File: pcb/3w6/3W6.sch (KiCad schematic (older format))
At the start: 115 parts, among them J1 USB_C Main, J2 USB_C I2C_L, J3 USB_C I2C_R, SW1 SW_Push, SW10 SW_Push, SW11 SW_Push, SW12 SW_Push, SW13 SW_Push, SW14 SW_Push, SW15 SW_Push, SW16 SW_Push, SW17 SW_Push, SW18 SW_Push, SW19 SW_Push, SW2 SW_Push, SW20 SW_Push, SW21 SW_Push, SW22 SW_Push, SW23 SW_Push, SW24 SW_Push, SW25 SW_Push, SW26 SW_Push, SW27 SW_Push, SW28 SW_Push, SW29 SW_Push, SW3 SW_Push, SW30 SW_Push, SW31 SW_Push, SW32 SW_Push, SW33 SW_Push, SW34 SW_Push, SW35 SW_Push, SW36 SW_Push, SW37 SW_Push, SW4 SW_Push, SW5 SW_Push, SW6 SW_Push, SW7 SW_Push, SW8 SW_Push, SW9 SW_Push, U2 TCA9555RTWR, U3 ATmega32U4-MU, Y1 16MHZ

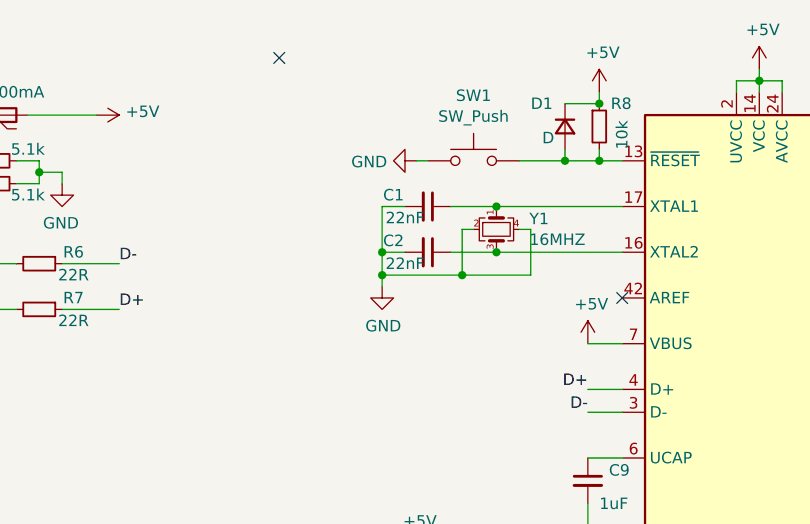
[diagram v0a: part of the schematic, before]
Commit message: fix library paths to use included part library fix wrong value for crystal condensators
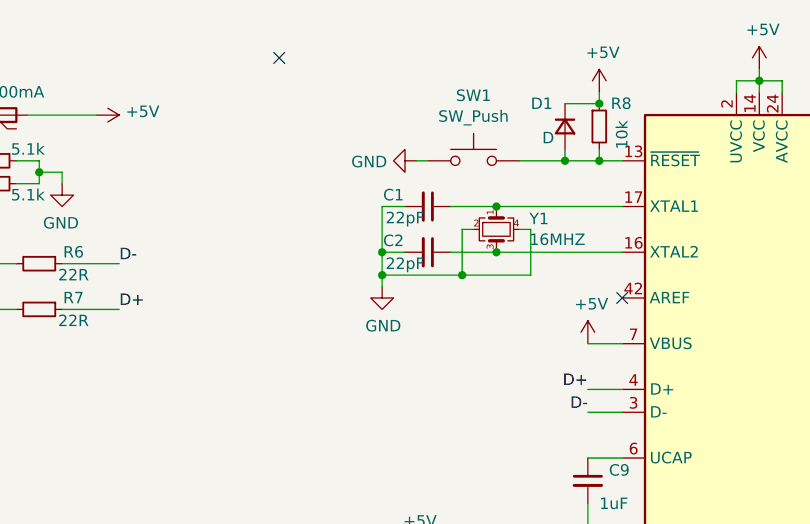
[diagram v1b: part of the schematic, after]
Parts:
- C1, C2: value 22nF -> 22pF; footprint WetCorn:C_0402_HandSolder -> Weteor:C_0402_HandSolder
- C3, C4, C5, C6, C7, C8, C9: footprint WetCorn:C_0402_HandSolder -> Weteor:C_0402_HandSolder
- D1, D10, D11, D12, D13, D14, D15, D16, D17, D18, D19, D2, D20, D21, D22, D23, D24, D25, D26, D27, D28, D29, D3, D30, D31, D32, D33, D34, D35, D36, D37, D38, D39, D4, D40, D41, D42, D43, D44, D45, D46, D47, D48, D49, D5, D50, D51, D52, D53, D6, D7, D8, D9: footprint WetCorn:D_SOD-123 -> Weteor:D_SOD-123
- J1, J2, J3: footprint WetCorn:USB-C-12-Pin-MidMount -> Weteor:USB-C-12-Pin-MidMount
- R1, R2, R3, R4, R5, R6, R7, R8, R9: footprint WetCorn:R_0402_HandSolder -> Weteor:R_0402_HandSolder
- SW1: footprint WetCorn:Micro_Push_Button_3x6x2.5mm -> Weteor:Micro_Push_Button_3x6x2.5mm
- SW10, SW11, SW12, SW13, SW14, SW15, SW16, SW17, SW18, SW19, SW2, SW20, SW21, SW22, SW23, SW24, SW25, SW26, SW27, SW28, SW29, SW3, SW30, SW31, SW32, SW34, SW35, SW36, SW4, SW5, SW6, SW7, SW8, SW9: footprint WetCorn:Kailh_Choc_1u -> Weteor:Kailh_Choc_1u
- SW33, SW37: footprint WetCorn:Kailh_Choc_1.5u -> Weteor:Kailh_Choc_1.5u

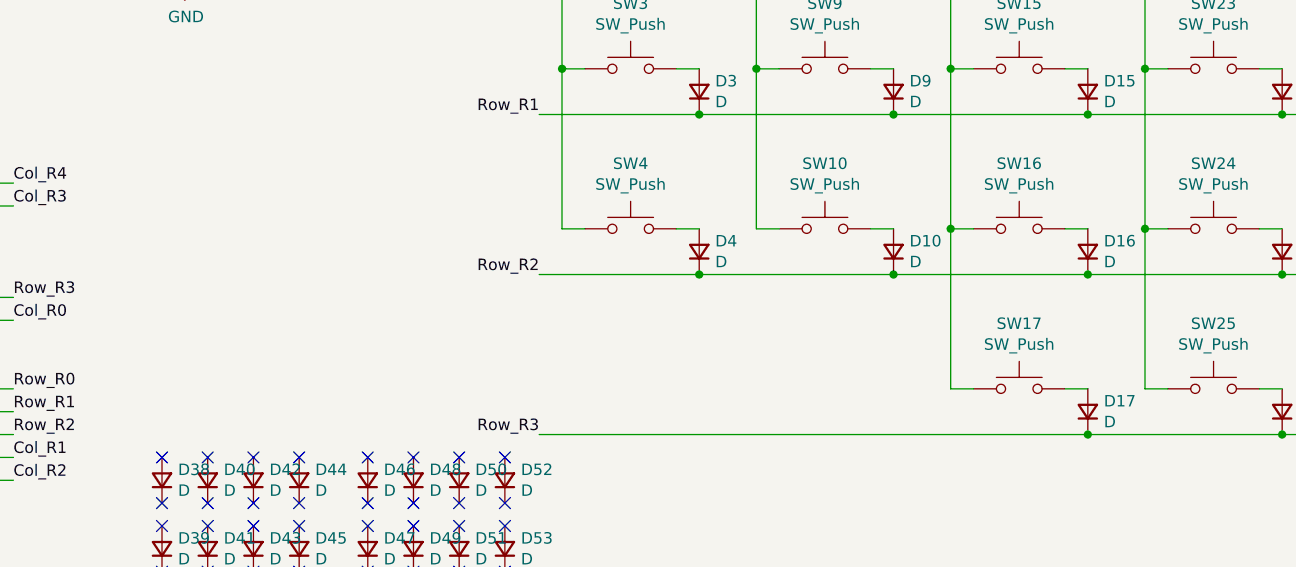
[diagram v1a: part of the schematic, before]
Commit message: add: Pimoroni Trackball support
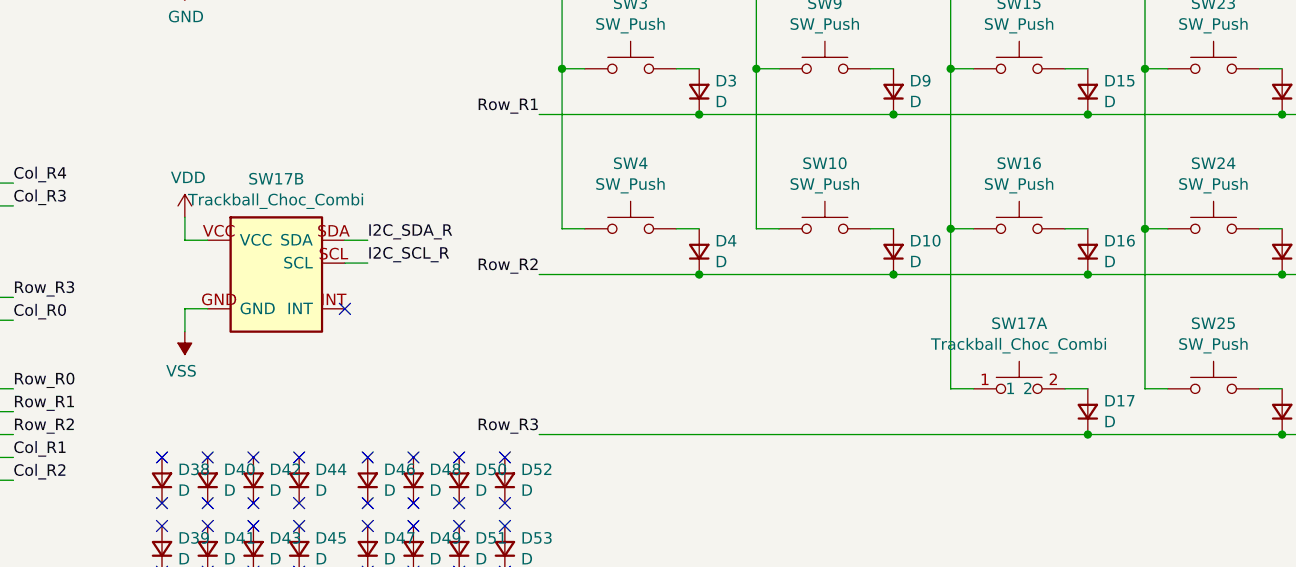
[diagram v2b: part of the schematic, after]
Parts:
- removed SW17: SW_Push, Weteor:Kailh_Choc_1u, symbol Switch:SW_Push
- added SW17: Trackball_Choc_Combi, Weteor:trackball_choc_combi, symbol weteor:Trackball_Choc_Combi
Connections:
- net Col_R2: now also SW17.1
- net I2C_SCL_R: now also SW17.SCL
- net I2C_SDA_R: now also SW17.SDA
- net VDD: now also SW17.VCC
- net VSS: now also SW17.GND
- net at D17.2 (A): now also SW17.2
- no-connect marks 68 -> 69
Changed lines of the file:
@@
-$EndComp
-$Comp
-L Switch:SW_Push SW17
-U 1 1 605A8206
-P 8900 6300
-F 0 "SW17" H 8900 6585 50  0000 C CNN
-F 1 "SW_Push" H 8900 6494 50  0000 C CNN
-F 2 "Weteor:Kailh_Choc_1u" H 8900 6500 50  0001 C CNN
-F 3 "~" H 8900 6500 50  0001 C CNN
-	1    8900 6300
-	1    0    0    -1
 $EndComp
 $Comp
@@
 	3650 5100 3650 5050
 $Comp
-L power:VDD #PWR012
-U 1 1 618443C9
-P 3650 4850
-F 0 "#PWR012" H 3650 4700 50  0001 C CNN
-F 1 "VDD" H 3665 5023 50  0000 C CNN
-F 2 "" H 3650 4850 50  0001 C CNN
-F 3 "" H 3650 4850 50  0001 C CNN
-	1    3650 4850
-	1    0    0    -1
-$EndComp
-$Comp
 L Device:C_Small C3
 U 1 1 6194E0AE
@@
 Connection ~ 3650 5050
 Wire Wire Line
-	3650 4850 3650 4950
-Wire Wire Line
 	3750 4950 3650 4950
-Connection ~ 3650 4950
 Wire Wire Line
 	3650 4950 3650 5050
@@
 NoConn ~ 5550 6900
 NoConn ~ 5550 7100
+Connection ~ 3650 4950
+Wire Wire Line
+	3650 4850 3650 4950
+$Comp
+L power:VDD #PWR012
+U 1 1 618443C9
+P 3650 4850
+F 0 "#PWR012" H 3650 4700 50  0001 C CNN
+F 1 "VDD" H 3665 5023 50  0000 C CNN
+F 2 "" H 3650 4850 50  0001 C CNN
+F 3 "" H 3650 4850 50  0001 C CNN
+	1    3650 4850
+	1    0    0    -1
+$EndComp
+$Comp
+L power:VDD #PWR0101
+U 1 1 60EC0F19
+P 5250 5550
+F 0 "#PWR0101" H 5250 5400 50  0001 C CNN
+F 1 "VDD" H 5265 5723 50  0000 C CNN
+F 2 "" H 5250 5550 50  0001 C CNN
+F 3 "" H 5250 5550 50  0001 C CNN
+	1    5250 5550
+	1    0    0    -1
+$EndComp
+$Comp
+L power:VSS #PWR0102
+U 1 1 60EC4385
+P 5250 6050
+F 0 "#PWR0102" H 5250 5900 50  0001 C CNN
+F 1 "VSS" H 5265 6223 50  0000 C CNN
+F 2 "" H 5250 6050 50  0001 C CNN
+F 3 "" H 5250 6050 50  0001 C CNN
+	1    5250 6050
+	-1   0    0    1
+$EndComp
+Wire Wire Line
+	5350 5950 5250 5950
+Wire Wire Line
+	5250 5950 5250 6050
+Wire Wire Line
+	5350 5650 5250 5650
+Wire Wire Line
+	5250 5650 5250 5550
+Wire Wire Line
+	5950 5650 6050 5650
+Wire Wire Line
+	5950 5750 6050 5750
+NoConn ~ 5950 5950
+Text Label 6050 5650 0    50   ~ 0
+I2C_SDA_R
+Text Label 6050 5750 0    50   ~ 0
+I2C_SCL_R
+$Comp
+L weteor:Trackball_Choc_Combi SW17
+U 2 1 60FEA571
+P 5650 5800
+F 0 "SW17" H 5650 6217 50  0000 C CNN
+F 1 "Trackball_Choc_Combi" H 5650 6126 50  0000 C CNN
+F 2 "Weteor:trackball_choc_combi" H 5650 6150 50  0001 C CNN
+F 3 "" H 5650 6150 50  0001 C CNN
+	2    5650 5800
+	1    0    0    -1
+$EndComp
+$Comp
+L weteor:Trackball_Choc_Combi SW17
+U 1 1 610E7D7F
+P 8900 6300
+F 0 "SW17" H 8900 6585 50  0000 C CNN
+F 1 "Trackball_Choc_Combi" H 8900 6494 50  0000 C CNN
+F 2 "" H 8900 6650 50  0001 C CNN
+F 3 "" H 8900 6650 50  0001 C CNN
+	1    8900 6300
+	1    0    0    -1
+$EndComp
 $EndSCHEMATC

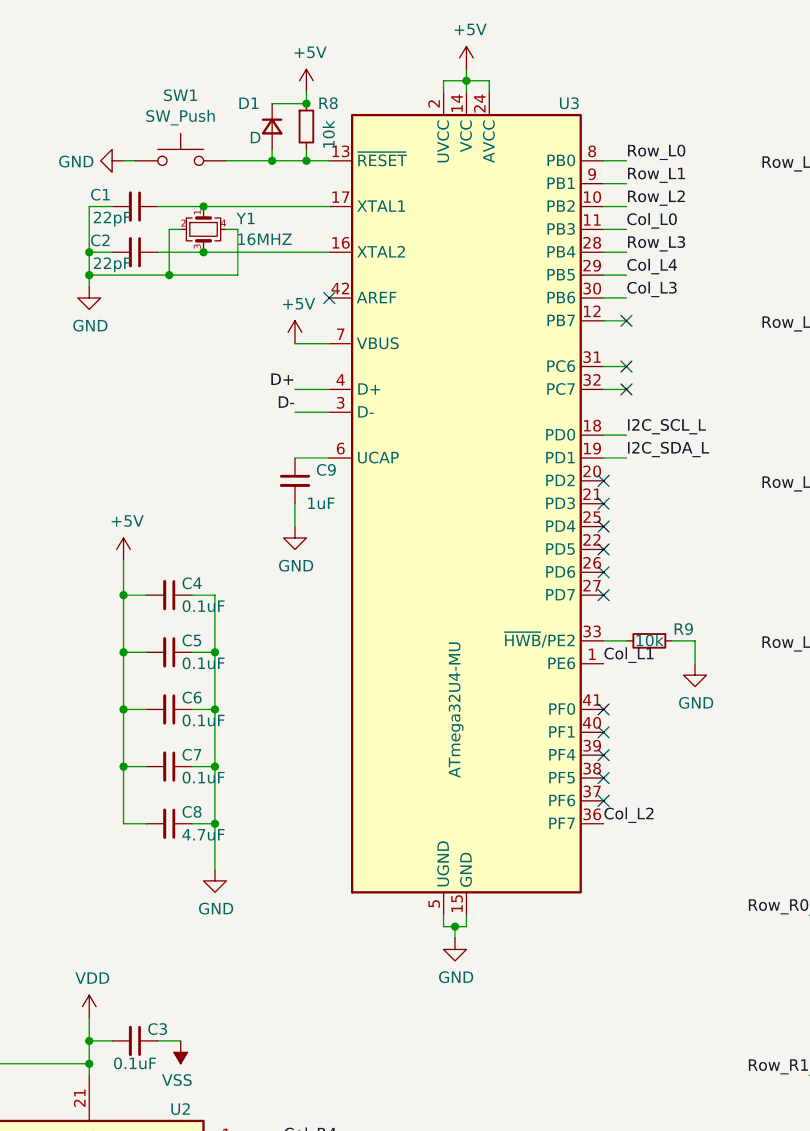
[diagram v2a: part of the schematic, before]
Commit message: chg: uses atmega32u4-AU now
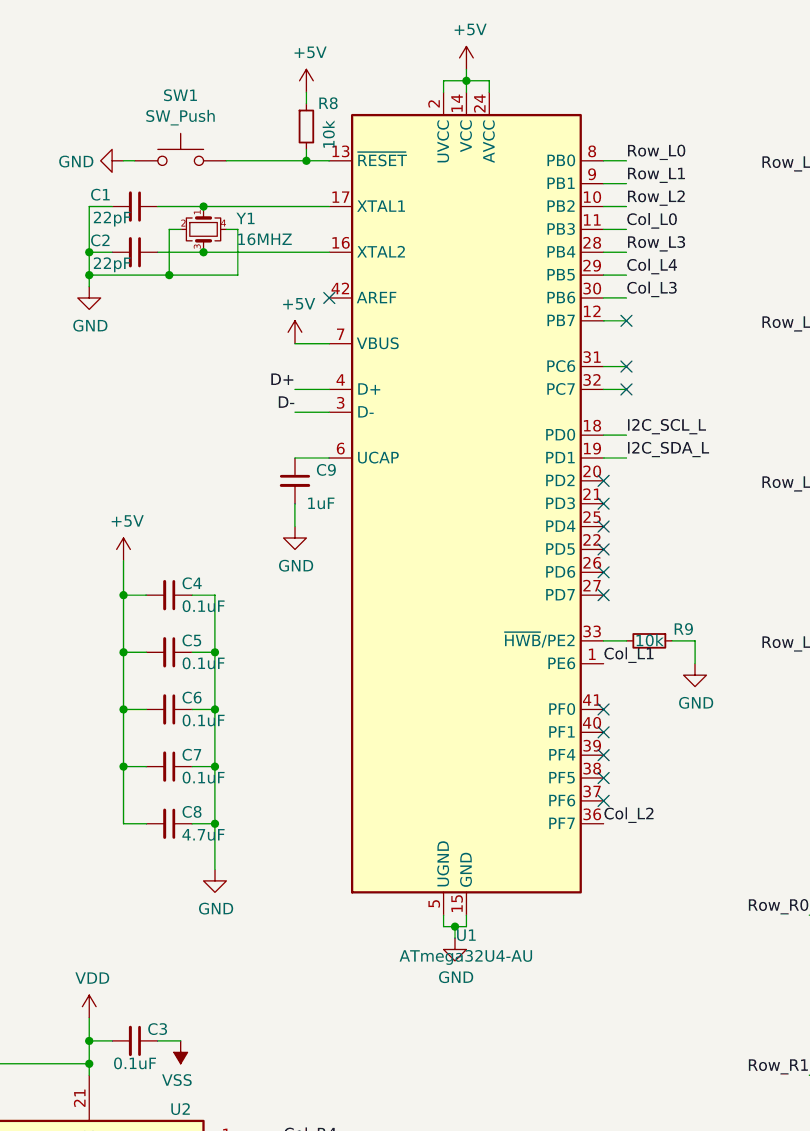
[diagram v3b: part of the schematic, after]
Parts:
- removed D1: D, Weteor:D_SOD-123, symbol Device:D_Small
- removed U3: ATmega32U4-MU, Package_DFN_QFN:QFN-44-1EP_7x7mm_P0.5mm_EP5.2x5.2mm, symbol MCU_Microchip_ATmega:ATmega32U4-MU
- added U1: ATmega32U4-AU, Package_QFP:TQFP-44_10x10mm_P0.8mm, symbol MCU_Microchip_ATmega:ATmega32U4-AU
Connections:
- net +5V: now also U1.14 (VCC), U1.2 (UVCC), U1.24 (AVCC), U1.34 (VCC), U1.44 (AVCC), U1.7 (VBUS)
- net Col_L0: now also U1.11 (PB3)
- net Col_L1: now also U1.1 (PE6)
- net Col_L2: now also U1.36 (PF7)
- net Col_L3: now also U1.30 (PB6)
- net Col_L4: now also U1.29 (PB5)
- net D+: now also U1.4 (D+)
- net D-: now also U1.3 (D-)
- net GND: now also U1.15 (GND), U1.23 (GND), U1.35 (GND), U1.43 (GND), U1.5 (UGND)
- net I2C_SCL_L: now also U1.18 (PD0)
- net I2C_SDA_L: now also U1.19 (PD1)
- net Row_L0: now also U1.8 (PB0)
- net Row_L1: now also U1.9 (PB1)
- net Row_L2: now also U1.10 (PB2)
- net Row_L3: now also U1.28 (PB4)
- net at R8.2, SW1.2: now also U1.13 (~RESET)
- net at C2.1, Y1.3: now also U1.16 (XTAL2)
- net at C1.1, Y1.1: now also U1.17 (XTAL1)
- net at R9.2: now also U1.33 (~HWB~/PE2)
- net at C9.1: now also U1.6 (UCAP)
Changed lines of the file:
@@
 NoConn ~ 1700 7000
 NoConn ~ 1700 7100
-$Comp
-L MCU_Microchip_ATmega:ATmega32U4-MU U3
-U 1 1 60BC96EF
-P 5300 2600
-F 0 "U3" H 5750 4350 50  0000 C CNN
-F 1 "ATmega32U4-MU" V 5250 1700 50  0000 C CNN
-F 2 "Package_DFN_QFN:QFN-44-1EP_7x7mm_P0.5mm_EP5.2x5.2mm" H 5300 2600 50  0001 C CIN
-F 3 "http://ww1.microchip.com/downloads/en/DeviceDoc/Atmel-7766-8-bit-AVR-ATmega16U4-32U4_Datasheet.pdf" H 5300 2600 50  0001 C CNN
-	1    5300 2600
-	1    0    0    -1
-$EndComp
 Wire Wire Line
 	4700 1300 4150 1300
@@
 Wire Wire Line
 	5250 4450 5300 4450
-$Comp
-L Device:D_Small D1
-U 1 1 610A7D05
-P 4450 950
-F 0 "D1" V 4350 1100 50  0000 R CNN
-F 1 "D" V 4500 1050 50  0000 R CNN
-F 2 "Weteor:D_SOD-123" V 4450 950 50  0001 C CNN
-F 3 "~" V 4450 950 50  0001 C CNN
-	1    4450 950
-	0    -1   1    0
-$EndComp
-Wire Wire Line
-	4450 850  4600 850
-Connection ~ 4600 850
-Wire Wire Line
-	4250 1100 4450 1100
 Connection ~ 4600 1100
-Wire Wire Line
-	4450 1050 4450 1100
-Connection ~ 4450 1100
-Wire Wire Line
-	4450 1100 4600 1100
 $Comp
 L Device:R_Small R9
@@
 	1    0    0    -1
 $EndComp
+$Comp
+L MCU_Microchip_ATmega:ATmega32U4-AU U1
+U 1 1 611A3CF9
+P 5300 2600
+F 0 "U1" H 5300 711 50  0000 C CNN
+F 1 "ATmega32U4-AU" H 5300 620 50  0000 C CNN
+F 2 "Package_QFP:TQFP-44_10x10mm_P0.8mm" H 5300 2600 50  0001 C CIN
+F 3 "http://ww1.microchip.com/downloads/en/DeviceDoc/Atmel-7766-8-bit-AVR-ATmega16U4-32U4_Datasheet.pdf" H 5300 2600 50  0001 C CNN
+	1    5300 2600
+	1    0    0    -1
+$EndComp
+Wire Wire Line
+	4250 1100 4600 1100
 $EndSCHEMATC
